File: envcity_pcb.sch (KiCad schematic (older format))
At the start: 0 parts

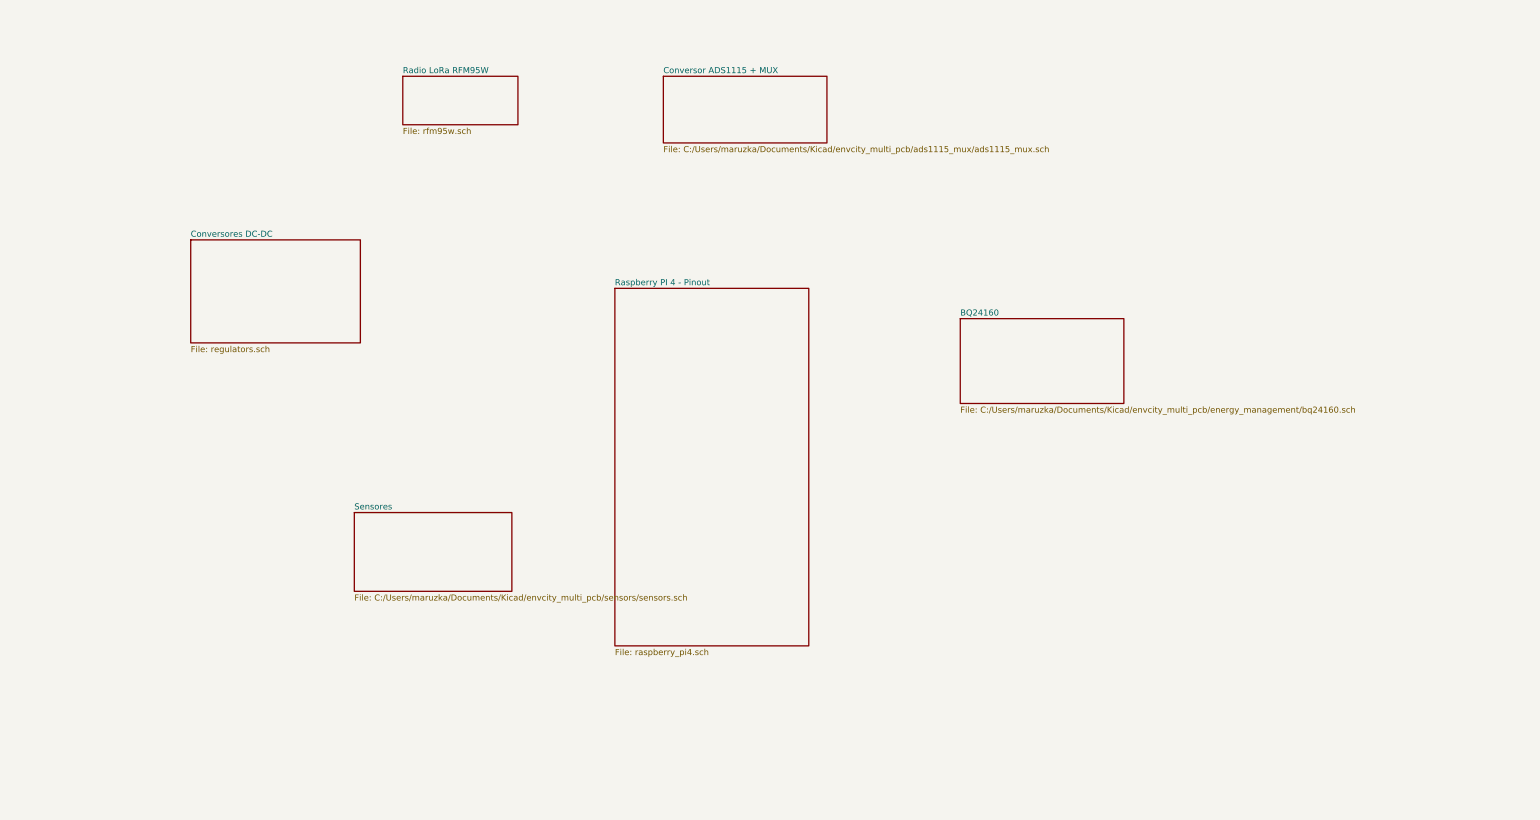
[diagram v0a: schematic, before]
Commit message: Conexão entre os componentes. Correção da lib do buck-boost. Separação do 3v3 da raspberry e do 3v3 do regulador
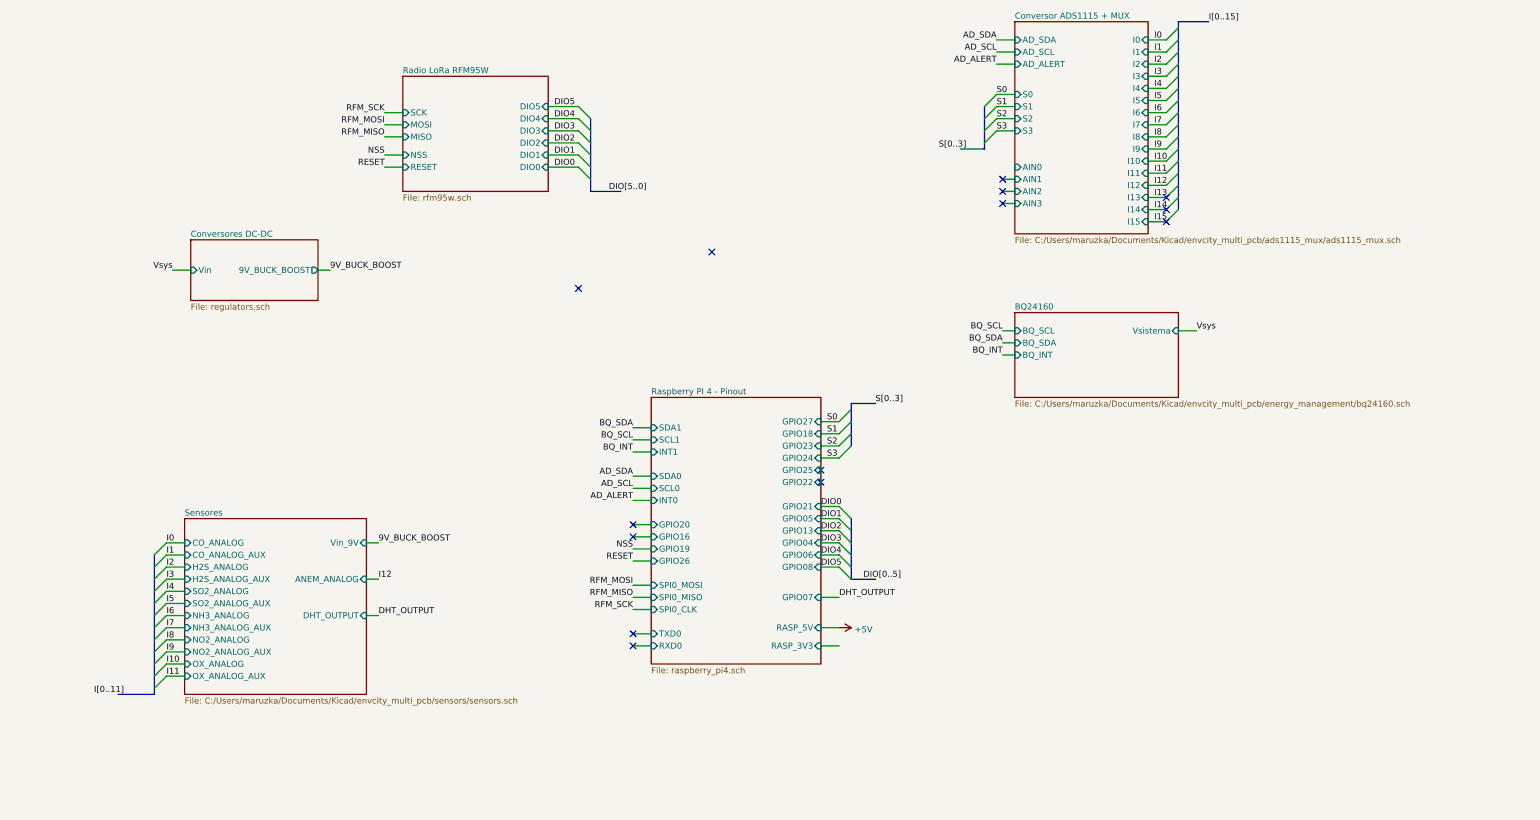
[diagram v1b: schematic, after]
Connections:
- no-connect marks 0 -> 14

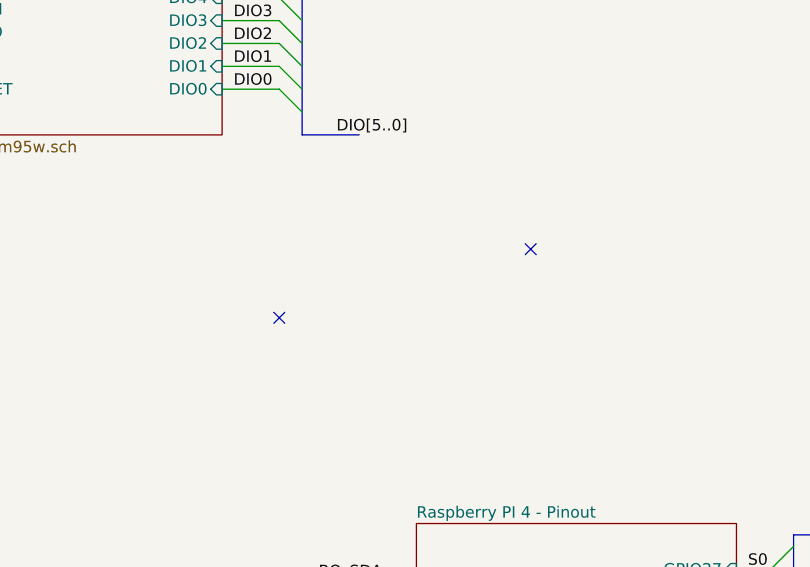
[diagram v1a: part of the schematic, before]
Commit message: Adicionando circuito para proteção de Vext_dc e Vusb; A explicação do circuito esta no esquematico
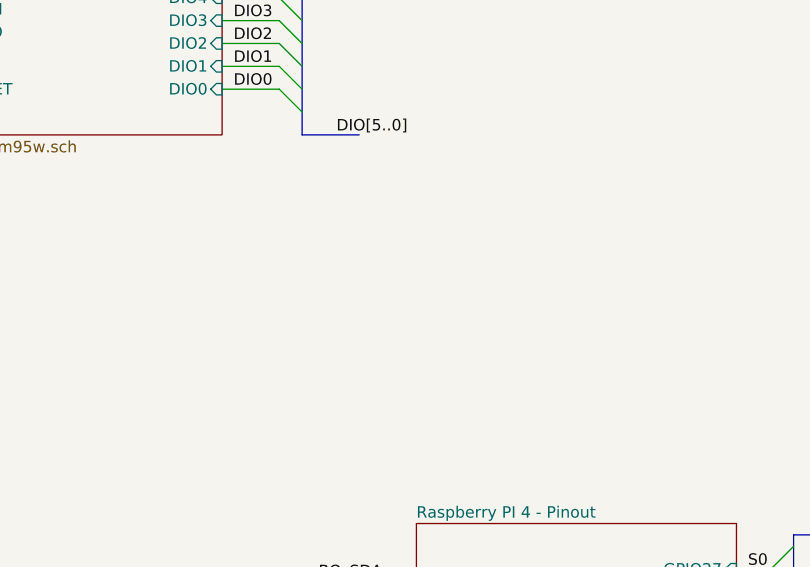
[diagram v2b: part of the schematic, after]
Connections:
- no-connect marks 14 -> 12
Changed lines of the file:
@@
 	0    1    1    0
 $EndComp
-NoConn ~ 5350 2950
-NoConn ~ 6450 2650
 Wire Bus Line
 	7600 4850 7600 5350

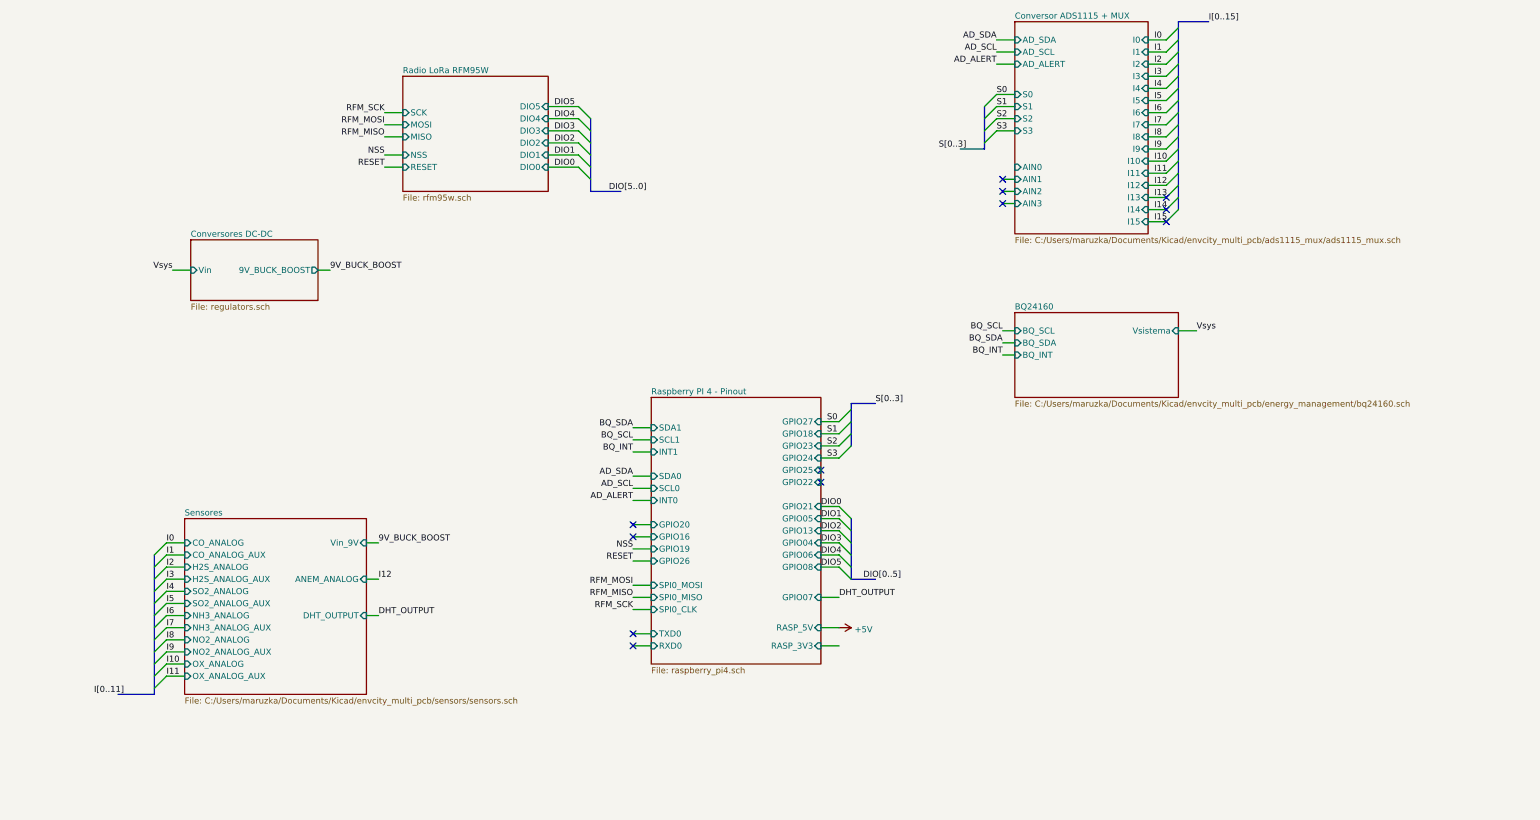
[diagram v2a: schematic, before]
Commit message: Add proteção contra reversao de polaridade no conector da bateria
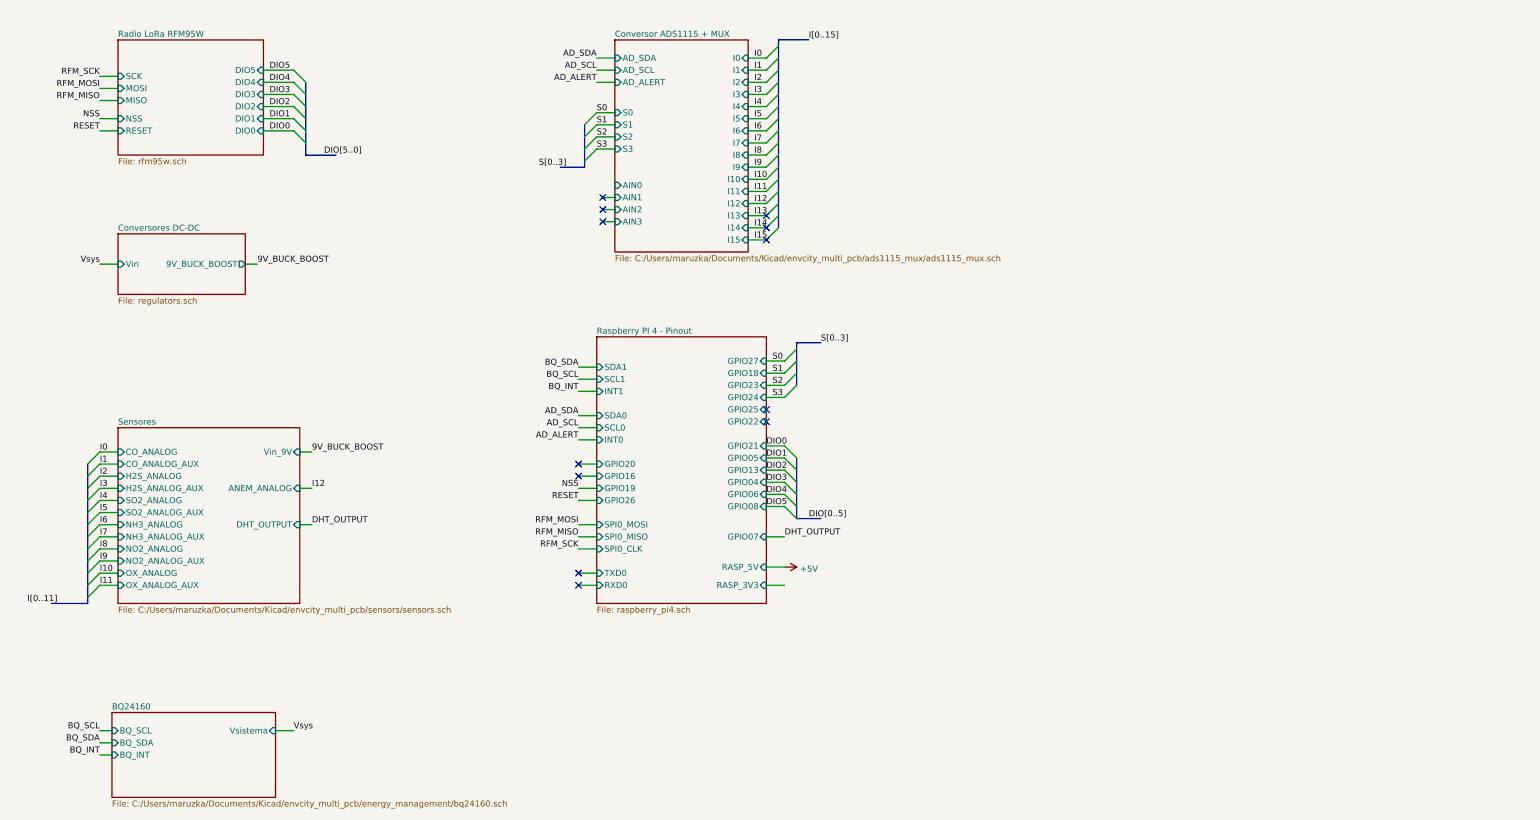
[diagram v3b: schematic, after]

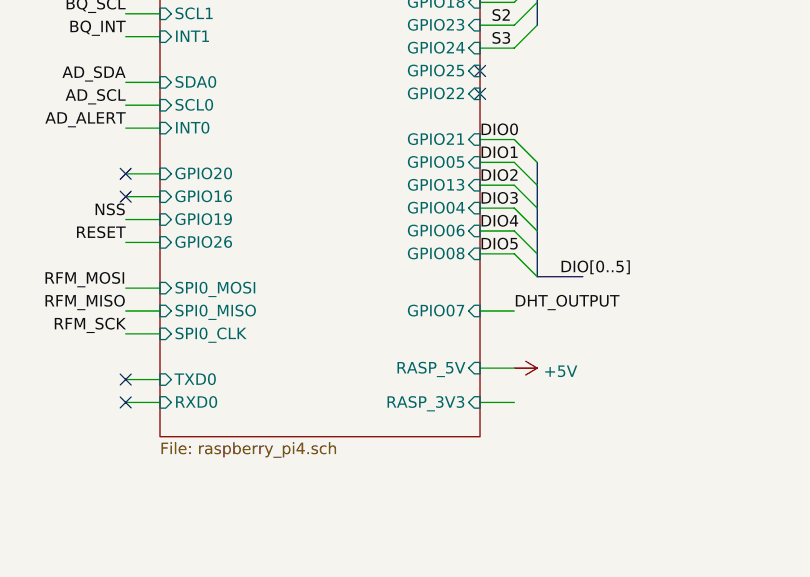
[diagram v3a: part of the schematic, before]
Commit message: Roteamento da PCB pronto; Agora o 3v3 da raspberry alimenta os resistores de pull up da comunicacao i2c do bq24160
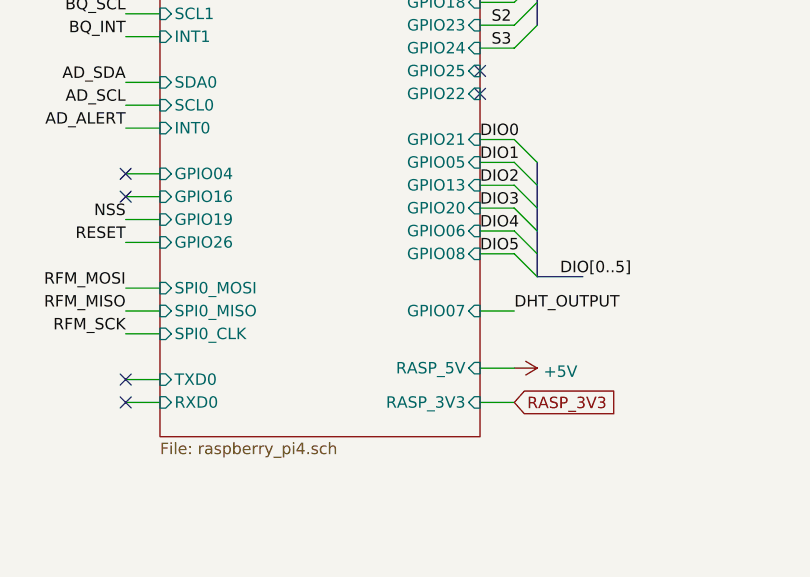
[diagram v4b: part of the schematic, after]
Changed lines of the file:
@@
 F6 "SDA0" I L 5500 4000 50
 F7 "INT0" I L 5500 4200 50
-F8 "GPIO20" I L 5500 4400 50
+F8 "GPIO20" I R 6900 4550 50
 F9 "GPIO16" I L 5500 4500 50
 F10 "GPIO19" I L 5500 4600 50
@@
 F24 "GPIO05" I R 6900 4350 50
 F25 "GPIO13" I R 6900 4450 50
-F26 "GPIO04" I R 6900 4550 50
+F26 "GPIO04" I L 5500 4400 50
 F27 "GPIO06" I R 6900 4650 50
 F28 "RASP_5V" I R 6900 5250 50
@@
 Wire Bus Line
 	7000 900  7000 2450
+Text GLabel 7050 5400 2    50   Input ~ 0
+RASP_3V3
 $EndSCHEMATC

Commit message: v3
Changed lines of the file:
@@
 $EndDescr
-$Sheet
-S 5500 3350 1400 2200
-U 61DBD0E2
-F0 "Raspberry PI 4 - Pinout" 50
-F1 "raspberry_pi4.sch" 50
-F2 "SDA1" I L 5500 3600 50
-F3 "SCL1" I L 5500 3700 50
-F4 "INT1" I L 5500 3800 50
-F5 "SCL0" I L 5500 4100 50
-F6 "SDA0" I L 5500 4000 50
-F7 "INT0" I L 5500 4200 50
-F8 "GPIO20" I R 6900 4550 50
-F9 "GPIO16" I L 5500 4500 50
-F10 "GPIO19" I L 5500 4600 50
-F11 "GPIO26" I L 5500 4700 50
-F12 "SPI0_MOSI" I L 5500 4900 50
-F13 "SPI0_MISO" I L 5500 5000 50
-F14 "SPI0_CLK" I L 5500 5100 50
-F15 "TXD0" I L 5500 5300 50
-F16 "RXD0" I L 5500 5400 50
-F17 "GPIO27" I R 6900 3550 50
-F18 "GPIO18" I R 6900 3650 50
-F19 "GPIO23" I R 6900 3750 50
-F20 "GPIO24" I R 6900 3850 50
-F21 "GPIO25" I R 6900 3950 50
-F22 "GPIO22" I R 6900 4050 50
-F23 "GPIO21" I R 6900 4250 50
-F24 "GPIO05" I R 6900 4350 50
-F25 "GPIO13" I R 6900 4450 50
-F26 "GPIO04" I L 5500 4400 50
-F27 "GPIO06" I R 6900 4650 50
-F28 "RASP_5V" I R 6900 5250 50
-F29 "RASP_3V3" I R 6900 5400 50
-F30 "GPIO08" I R 6900 4750 50
-F31 "GPIO07" I R 6900 5000 50
-$EndSheet
 $Sheet
 S 1550 2500 1050 500
@@
 	1550 2750 1400 2750
 $Comp
-L power:+5V #PWR0101
+L power:+5V #PWR01
 U 1 1 61FD7E9B
 P 7050 5250
-F 0 "#PWR0101" H 7050 5100 50  0001 C CNN
+F 0 "#PWR01" H 7050 5100 50  0001 C CNN
 F 1 "+5V" V 7065 5378 50  0000 L CNN
 F 2 "" H 7050 5250 50  0001 C CNN
@@
 Text GLabel 7050 5400 2    50   Input ~ 0
 RASP_3V3
+$Sheet
+S 5500 3350 1400 2200
+U 61DBD0E2
+F0 "Raspberry PI 4 - Pinout" 50
+F1 "C:/Users/maruzka/Documents/Kicad/envcity_multi_pcb/raspberrypi4/raspberrypi4.sch" 50
+F2 "SDA1" I L 5500 3600 50
+F3 "SCL1" I L 5500 3700 50
+F4 "INT1" I L 5500 3800 50
+F5 "SCL0" I L 5500 4100 50
+F6 "SDA0" I L 5500 4000 50
+F7 "INT0" I L 5500 4200 50
+F8 "GPIO20" I R 6900 4550 50
+F9 "GPIO16" I L 5500 4500 50
+F10 "GPIO19" I L 5500 4600 50
+F11 "GPIO26" I L 5500 4700 50
+F12 "SPI0_MOSI" I L 5500 4900 50
+F13 "SPI0_MISO" I L 5500 5000 50
+F14 "SPI0_CLK" I L 5500 5100 50
+F15 "TXD0" I L 5500 5300 50
+F16 "RXD0" I L 5500 5400 50
+F17 "GPIO27" I R 6900 3550 50
+F18 "GPIO18" I R 6900 3650 50
+F19 "GPIO23" I R 6900 3750 50
+F20 "GPIO24" I R 6900 3850 50
+F21 "GPIO25" I R 6900 3950 50
+F22 "GPIO22" I R 6900 4050 50
+F23 "GPIO21" I R 6900 4250 50
+F24 "GPIO05" I R 6900 4350 50
+F25 "GPIO13" I R 6900 4450 50
+F26 "GPIO04" I L 5500 4400 50
+F27 "GPIO06" I R 6900 4650 50
+F28 "RASP_5V" I R 6900 5250 50
+F29 "RASP_3V3" I R 6900 5400 50
+F30 "GPIO08" I R 6900 4750 50
+F31 "GPIO07" I R 6900 5000 50
+$EndSheet
 Wire Bus Line
 	7150 4350 7150 4850
